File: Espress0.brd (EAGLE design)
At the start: 36.8 x 39.4 mm, 41 parts, among them CN1 4U#20329, Q2 reset, U1 AP2112K-3.3, U2 2MB Flash, U3 MCP73831T-2ACI/OT

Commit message: Add files via upload
* Fix micro USB grounding plane
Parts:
- moved CN1 0.38 mm to (18.4, 4.70)
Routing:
- net GND: track 8.82 -> 11.7 mm
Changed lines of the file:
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@@
 <attribute name="VALUE" x="19.177" y="12.319" size="0.4064" layer="121" ratio="10" rot="R90"/>
 </element>
-<element name="CN1" library="microbuilder" package="4UCONN_20329_V2" value="4U#20329" x="18.415" y="4.318"/>
+<element name="CN1" library="microbuilder" package="4UCONN_20329_V2" value="4U#20329" x="18.415" y="4.699"/>
 <element name="D2" library="adafruit" package="SOD-123FL" value="SCHOTTKY" x="23.622" y="10.668" smashed="yes" rot="R180">
 <attribute name="NAME" x="22.268" y="9.128" size="0.4064" layer="121"/>
@@
 </element>
 <element name="R1" library="microbuilder" package="0603-NO" value="1.5K" x="8.598803125" y="3.720196875" smashed="yes" rot="R269.6">
-<attribute name="NAME" x="9.9633375" y="5.520884375" size="0.6096" layer="25" font="vector" ratio="18" rot="R89.6"/>
-<attribute name="VALUE" x="8.08241875" y="5.51100625" size="0.4064" layer="121" font="vector" ratio="10" rot="R359.6"/>
+<attribute name="NAME" x="7.560115625" y="4.3753375" size="0.6096" layer="25" font="vector" ratio="18" rot="R179.6"/>
+<attribute name="VALUE" x="6.43141875" y="4.74900625" size="0.4064" layer="121" font="vector" ratio="10" rot="R359.6"/>
 </element>
 <element name="R4" library="microbuilder" package="0603-NO" value="10K" x="23.368" y="20.955" smashed="yes" rot="R180">
@@
 </element>
 <element name="R5" library="microbuilder" package="0603-NO" value="10K" x="7.239" y="7.747" smashed="yes" rot="R180">
-<attribute name="NAME" x="5.588" y="8.001" size="0.6096" layer="121" font="vector" ratio="18" rot="R180"/>
+<attribute name="NAME" x="5.715" y="9.017" size="0.6096" layer="121" font="vector" ratio="18" rot="R180"/>
 <attribute name="VALUE" x="7.62" y="6.985" size="0.4064" layer="121" font="vector" ratio="10" rot="R180"/>
 </element>
@@
 <element name="U2" library="microbuilder" package="SOIC8_208MIL" value="2MB Flash" x="9.652" y="11.684" smashed="yes" rot="R90">
 <attribute name="NAME" x="13.081" y="8.509" size="0.6096" layer="121" ratio="18" rot="R359.3"/>
-<attribute name="VALUE" x="7.239" y="15.113" size="0.4064" layer="121" ratio="10" rot="R180"/>
+<attribute name="VALUE" x="7.874" y="14.986" size="0.4064" layer="121" ratio="10" rot="R180"/>
 </element>
 <element name="PA22" library="testpad" package="B1,27" value="TPB1,27" x="13.716" y="7.62" smashed="yes">
-<attribute name="NAME" x="16.256" y="7.747" size="0.4064" layer="121" ratio="10" rot="R180"/>
+<attribute name="NAME" x="13.081" y="6.858" size="0.4064" layer="121" ratio="10" rot="R180"/>
 <attribute name="TP_SIGNAL_NAME" value="" x="13.081" y="5.715" size="1" layer="37"/>
 <attribute name="VALUE" x="13.081" y="6.858" size="0.0254" layer="27"/>
@@
 <via x="8.763" y="18.034" extent="1-16" drill="0.5"/>
 <via x="15.748" y="24.892" extent="1-16" drill="0.5"/>
-<wire x1="15.115" y1="5.218" x2="15.73768125" y2="5.103025" width="0.3048" layer="1"/>
 <wire x1="15.113" y1="25.908" x2="15.748" y2="24.892" width="0.508" layer="1"/>
 <via x="11.303" y="29.845" extent="1-16" drill="0.5"/>
-<wire x1="14.815" y1="2.418" x2="12.822" y2="2.418" width="0.508" layer="1"/>
-<wire x1="22.015" y1="2.418" x2="24.008" y2="2.418" width="0.508" layer="1"/>
-<wire x1="19.715" y1="5.093" x2="19.715" y2="4.094" width="0.4064" layer="1"/>
-<wire x1="19.165" y1="3.544" x2="19.165" y2="2.318" width="0.4064" layer="1"/>
+<wire x1="19.715" y1="5.474" x2="19.715" y2="4.094" width="0.4064" layer="1"/>
+<wire x1="19.165" y1="3.544" x2="19.165" y2="2.699" width="0.4064" layer="1"/>
 <wire x1="19.715" y1="4.094" x2="19.165" y2="3.544" width="0.4064" layer="1"/>
+<wire x1="19.265" y1="2.799" x2="19.165" y2="2.699" width="0.508" layer="1"/>
+<wire x1="14.815" y1="2.799" x2="14.815" y2="2.667" width="0.508" layer="1"/>
+<wire x1="22.015" y1="2.799" x2="14.815" y2="2.799" width="0.508" layer="1"/>
+<wire x1="19.715" y1="4.094" x2="22.015" y2="2.799" width="0" layer="19" extent="1-1"/>
 </signal>
 <signal name="D+">
 <contactref element="CN1" pad="D+"/>
 <contactref element="ATSAMD21E" pad="24"/>
-<wire x1="18.415" y1="13.716" x2="18.415" y2="5.093" width="0.3048" layer="1"/>
+<wire x1="18.415" y1="13.716" x2="18.415" y2="5.474" width="0.3048" layer="1"/>
 <wire x1="16.863" y1="23.408" x2="16.863" y2="15.268" width="0.3048" layer="1"/>
 <wire x1="16.863" y1="15.268" x2="18.415" y2="13.716" width="0.3048" layer="1"/>
@@
 <contactref element="ATSAMD21E" pad="23"/>
 <wire x1="16.363" y1="12.974" x2="17.8034" y2="11.5336" width="0.3556" layer="1"/>
-<wire x1="17.765" y1="5.093" x2="17.8034" y2="5.1314" width="0.3556" layer="1"/>
+<wire x1="17.765" y1="5.474" x2="17.8034" y2="5.1314" width="0.3556" layer="1"/>
 <wire x1="17.8034" y1="5.1314" x2="17.8034" y2="11.5336" width="0.3556" layer="1"/>
 <wire x1="16.363" y1="23.408" x2="16.363" y2="12.974" width="0.3048" layer="1"/>
@@
 <wire x1="30.099" y1="17.272" x2="27.559" y2="17.272" width="0.508" layer="16"/>
 <wire x1="17.115" y1="6.253" x2="16.51" y2="6.858" width="0.508" layer="1"/>
-<wire x1="17.115" y1="5.093" x2="17.115" y2="6.253" width="0.508" layer="1"/>
+<wire x1="17.115" y1="5.474" x2="17.115" y2="6.253" width="0.508" layer="1"/>
 <wire x1="27.559" y1="17.272" x2="20.955" y2="10.668" width="0.508" layer="16"/>
 <wire x1="20.955" y1="10.668" x2="19.939" y2="10.668" width="0.508" layer="16"/>
@@
 <wire x1="17.613" y1="24.658" x2="18.268" y2="24.658" width="0.3048" layer="1"/>
 <wire x1="18.268" y1="24.658" x2="18.669" y2="24.257" width="0.3048" layer="1"/>
-<wire x1="18.669" y1="24.257" x2="18.669" y2="20.193" width="0.3048" layer="1"/>
+<wire x1="18.669" y1="24.257" x2="18.669" y2="22.86" width="0.3048" layer="1"/>
+<wire x1="18.669" y1="22.86" x2="18.669" y2="20.193" width="0.3048" layer="1"/>
 <wire x1="18.669" y1="20.193" x2="24.003" y2="20.193" width="0.3048" layer="16"/>
 <wire x1="24.003" y1="20.193" x2="34.29" y2="30.48" width="0.3048" layer="16"/>
@@
 <contactref element="U2" pad="2"/>
 <contactref element="ATSAMD21E" pad="20"/>
-<wire x1="14.863" y1="23.408" x2="14.863" y2="11.43" width="0.3048" layer="1"/>
+<wire x1="14.863" y1="23.408" x2="14.863" y2="22.86" width="0.3048" layer="1"/>
+<wire x1="14.863" y1="22.86" x2="14.863" y2="11.43" width="0.3048" layer="1"/>
 <wire x1="13.843" y1="11.049" x2="12.967" y2="11.049" width="0.3556" layer="1"/>
 <wire x1="14.863" y1="11.43" x2="14.482" y2="11.049" width="0.3048" layer="1"/>
@@
 <wire x1="16.498" y1="11.188" x2="16.51" y2="10.922" width="0.3556" layer="16"/>
 <wire x1="16.51" y1="10.922" x2="16.51" y2="9.652" width="0.3556" layer="16"/>
-<wire x1="15.863" y1="23.408" x2="15.863" y2="11.823" width="0.254" layer="1"/>
+<wire x1="15.863" y1="23.408" x2="15.863" y2="22.86" width="0.254" layer="1"/>
+<wire x1="15.863" y1="22.86" x2="15.863" y2="11.823" width="0.254" layer="1"/>
 <wire x1="15.863" y1="11.823" x2="16.498" y2="11.188" width="0.254" layer="1"/>
 </signal>
@@
 <contactref element="PA22" pad="TP"/>
 <contactref element="ATSAMD21E" pad="21"/>
-<wire x1="15.363" y1="23.408" x2="15.363" y2="9.394" width="0.254" layer="1"/>
+<wire x1="15.363" y1="23.408" x2="15.363" y2="22.86" width="0.254" layer="1"/>
+<wire x1="15.363" y1="22.86" x2="15.363" y2="9.394" width="0.254" layer="1"/>
 <wire x1="15.363" y1="9.394" x2="13.716" y2="7.747" width="0.254" layer="1"/>
 <wire x1="13.716" y1="7.747" x2="13.716" y2="7.62" width="0.254" layer="1"/>
@@
 <via x="13.22" y="16.395" extent="1-16" drill="0.5"/>
 <wire x1="13.22" y1="16.395" x2="14.363" y2="17.538" width="0.254" layer="1"/>
-<wire x1="14.363" y1="17.538" x2="14.363" y2="23.408" width="0.254" layer="1"/>
+<wire x1="14.363" y1="17.538" x2="14.363" y2="22.86" width="0.254" layer="1"/>
+<wire x1="14.363" y1="22.86" x2="14.363" y2="23.408" width="0.254" layer="1"/>
 <wire x1="13.22" y1="16.395" x2="14.605" y2="15.01" width="0.3556" layer="16"/>
 <wire x1="14.605" y1="15.01" x2="14.605" y2="14.859" width="0.3556" layer="16"/>
@@
 <wire x1="19.558" y1="30.861" x2="28.956" y2="30.861" width="0.3556" layer="1"/>
 </signal>
+<signal name="N$3">
+<via x="19.685" y="8.255" extent="1-16" drill="0.35"/>
+</signal>
 </signals>

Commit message: Add files via upload
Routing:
- net GND: track 11.7 -> 10.4 mm
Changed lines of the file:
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@@
 <wire x1="19.265" y1="2.799" x2="19.165" y2="2.699" width="0.508" layer="1"/>
 <wire x1="14.815" y1="2.799" x2="14.815" y2="2.667" width="0.508" layer="1"/>
-<wire x1="22.015" y1="2.799" x2="14.815" y2="2.799" width="0.508" layer="1"/>
-<wire x1="19.715" y1="4.094" x2="22.015" y2="2.799" width="0" layer="19" extent="1-1"/>
+<wire x1="22.015" y1="2.799" x2="22.015" y2="2.699" width="0.508" layer="1"/>
+<wire x1="22.015" y1="2.699" x2="19.165" y2="2.699" width="0.508" layer="1"/>
+<wire x1="14.815" y1="2.799" x2="14.815" y2="2.699" width="0.508" layer="1"/>
+<wire x1="14.815" y1="2.699" x2="17.665" y2="2.699" width="0.508" layer="1"/>
 </signal>
 <signal name="D+">

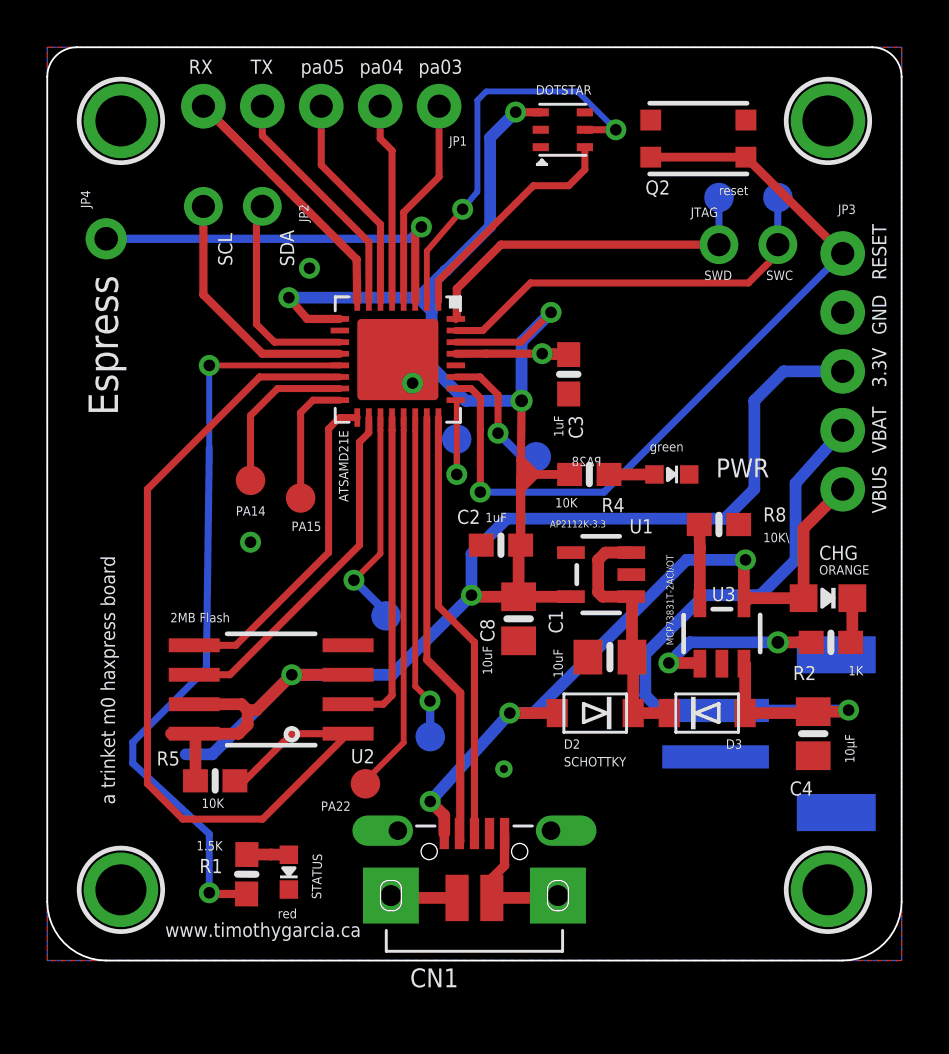
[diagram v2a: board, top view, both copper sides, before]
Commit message: Add files via upload
* SPI flash trace updates
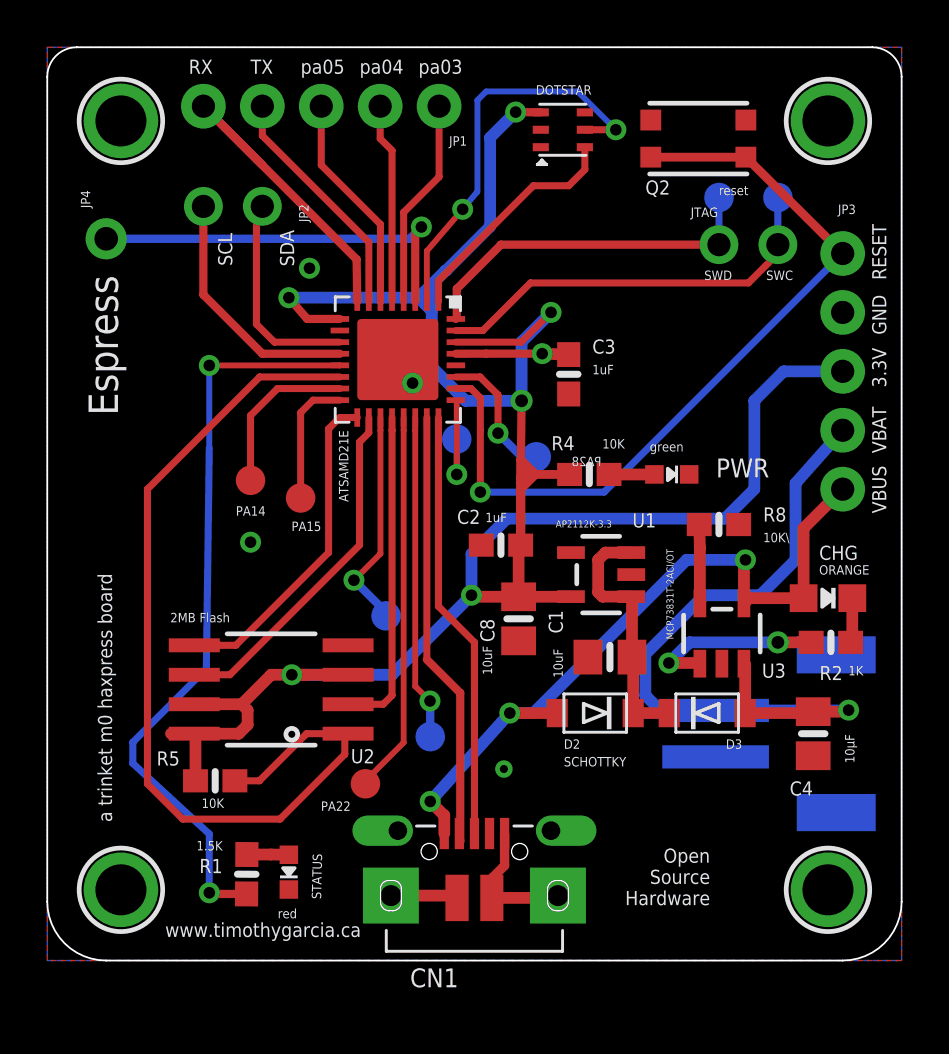
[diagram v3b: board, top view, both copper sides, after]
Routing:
- net 3.3V: track 107.2 -> 101.4 mm
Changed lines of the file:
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@@
 <text x="7.366" y="31.369" size="0.6096" layer="121" font="vector" rot="R270">SCL</text>
 <text x="3.048" y="23.495" size="1.27" layer="121" font="fixed" rot="R90">Espress</text>
-<text x="2.54" y="29.21" size="0.6096" layer="122" rot="MR270">Based on Trinket m0 by Adafruit Industries.</text>
+<text x="30.861" y="36.195" size="0.6096" layer="122" font="fixed" rot="MR0">Based on Trinket m0
+by Adafruit Industries.</text>
 <text x="31.496" y="1.143" size="0.6096" layer="122" rot="MR0">04/2018 - v0.3</text>
 <text x="5.08" y="1.016" size="0.6096" layer="121">www.timothygarcia.ca</text>
@@
 <text x="35.56" y="31.75" size="0.6096" layer="121" font="fixed" rot="R270">RESET</text>
 <text x="35.56" y="28.702" size="0.6096" layer="121" font="vector" rot="R270">GND</text>
-<text x="2.921" y="6.731" size="0.6096" layer="121" rot="R90">a trinket m0 haxpress board</text>
-<text x="3.81" y="29.21" size="0.6096" layer="122" rot="MR270.6">Designed for CircuitPython, but works with Arduino too!</text>
-<text x="30.861" y="37.338" size="0.6096" layer="122" rot="MR0">Open Source Hardware</text>
+<text x="2.794" y="5.969" size="0.6096" layer="121" rot="R90">a trinket m0 haxpress board</text>
+<text x="2.794" y="29.21" size="0.6096" layer="122" rot="MR270.6">Designed for CircuitPython, but works with Arduino too!</text>
+<text x="28.575" y="4.826" size="0.6096" layer="121" rot="R180">Open
+Source
+Hardware</text>
 <text x="35.56" y="21.336" size="0.6096" layer="121" font="fixed" rot="R270">VBUS</text>
 <wire x1="0" y1="2.54" x2="2.54" y2="0" width="0.0762" layer="20" curve="90"/>
@@
 </element>
 <element name="C3" library="microbuilder" package="0603-NO" value="1uF" x="22.479" y="25.273" smashed="yes" rot="R270">
-<attribute name="NAME" x="22.478996875" y="23.494996875" size="0.6096" layer="121" font="vector" ratio="18" rot="R270"/>
-<attribute name="VALUE" x="21.843996875" y="23.494996875" size="0.4064" layer="121" font="vector" ratio="10" rot="R270"/>
+<attribute name="NAME" x="23.495003125" y="26.161996875" size="0.6096" layer="121" font="vector" ratio="18"/>
+<attribute name="VALUE" x="23.495003125" y="25.272996875" size="0.4064" layer="121" font="vector" ratio="10"/>
 </element>
 <element name="C8" library="microbuilder" package="0805-NO" value="10uF" x="20.32" y="14.732" smashed="yes" rot="R270">
@@
 </element>
 <element name="R4" library="microbuilder" package="0603-NO" value="10K" x="23.368" y="20.955" smashed="yes" rot="R180">
-<attribute name="NAME" x="24.892" y="19.939" size="0.6096" layer="121" font="vector" ratio="18" rot="R180"/>
-<attribute name="VALUE" x="22.86" y="19.939" size="0.4064" layer="121" font="vector" ratio="10" rot="R180"/>
+<attribute name="NAME" x="22.733" y="22.606" size="0.6096" layer="121" font="vector" ratio="18" rot="R180"/>
+<attribute name="VALUE" x="24.892" y="22.479" size="0.4064" layer="121" font="vector" ratio="10" rot="R180"/>
 </element>
 <element name="R5" library="microbuilder" package="0603-NO" value="10K" x="7.239" y="7.747" smashed="yes" rot="R180">
@@
 </element>
 <element name="U1" library="microbuilder" package="SOT23-5" value="AP2112K-3.3" x="23.876" y="16.637" smashed="yes" rot="R90">
-<attribute name="NAME" x="25.092" y="18.415" size="0.6096" layer="25" ratio="18"/>
-<attribute name="VALUE" x="21.663" y="18.669" size="0.3048" layer="121" ratio="10"/>
+<attribute name="NAME" x="25.219" y="18.669" size="0.6096" layer="25" ratio="18"/>
+<attribute name="VALUE" x="21.917" y="18.669" size="0.3048" layer="121" ratio="10"/>
 </element>
 <element name="U2" library="microbuilder" package="SOIC8_208MIL" value="2MB Flash" x="9.652" y="11.684" smashed="yes" rot="R90">
@@
 </element>
 <element name="U3" library="microbuilder" package="SOT23-5" value="MCP73831T-2ACI/OT" x="29.083" y="14.097" smashed="yes">
-<attribute name="NAME" x="28.648" y="15.494" size="0.6096" layer="121" ratio="18"/>
-<attribute name="VALUE" x="26.997" y="13.589" size="0.3048" layer="121" ratio="10" rot="R90"/>
+<attribute name="NAME" x="30.807" y="12.192" size="0.6096" layer="121" ratio="18"/>
+<attribute name="VALUE" x="26.997" y="13.843" size="0.3048" layer="121" ratio="10" rot="R90"/>
 </element>
 <element name="CHG" library="microbuilder" package="CHIPLED_0805_NOOUTLINE" value="ORANGE" x="33.655" y="15.621" smashed="yes" rot="R270">
@@
 </element>
 <element name="R2" library="microbuilder" package="0603-NO" value="1K" x="33.782" y="13.716" smashed="yes" rot="R180">
-<attribute name="NAME" x="33.147" y="12.7" size="0.6096" layer="121" font="vector" ratio="18" rot="R180"/>
+<attribute name="NAME" x="34.29" y="12.7" size="0.6096" layer="121" font="vector" ratio="18" rot="R180"/>
 <attribute name="VALUE" x="35.179" y="12.7" size="0.4064" layer="121" font="vector" ratio="10" rot="R180"/>
 </element>
@@
 <wire x1="19.715" y1="4.094" x2="19.165" y2="3.544" width="0.4064" layer="1"/>
 <wire x1="19.265" y1="2.799" x2="19.165" y2="2.699" width="0.508" layer="1"/>
-<wire x1="14.815" y1="2.799" x2="14.815" y2="2.667" width="0.508" layer="1"/>
 <wire x1="22.015" y1="2.799" x2="22.015" y2="2.699" width="0.508" layer="1"/>
 <wire x1="22.015" y1="2.699" x2="19.165" y2="2.699" width="0.508" layer="1"/>
-<wire x1="14.815" y1="2.799" x2="14.815" y2="2.699" width="0.508" layer="1"/>
-<wire x1="14.815" y1="2.699" x2="17.665" y2="2.699" width="0.508" layer="1"/>
+<wire x1="14.815" y1="2.799" x2="17.665" y2="2.799" width="0.508" layer="1"/>
+<wire x1="17.665" y1="2.799" x2="17.665" y2="2.699" width="0.508" layer="1"/>
 </signal>
 <signal name="D+">
@@
 <via x="20.447" y="24.13" extent="1-16" drill="0.55"/>
 <contactref element="JP3" pad="3"/>
-<wire x1="10.541" y1="12.319" x2="7.112" y2="8.89" width="0.508" layer="16"/>
-<wire x1="7.112" y1="8.89" x2="5.969" y2="8.89" width="0.508" layer="16"/>
 <via x="20.193" y="36.576" extent="1-16" drill="0.5"/>
 <wire x1="21.275" y1="36.564" x2="20.193" y2="36.576" width="0.3556" layer="1"/>
@@
 <wire x1="8.636" y1="10.16" x2="8.255" y2="9.779" width="0.508" layer="1"/>
 <wire x1="8.255" y1="9.779" x2="6.337" y2="9.779" width="0.508" layer="1"/>
-<wire x1="10.541" y1="12.319" x2="9.017" y2="10.795" width="0.508" layer="1"/>
-<wire x1="9.017" y1="10.795" x2="8.636" y2="10.795" width="0.508" layer="1"/>
 <wire x1="16.5735" y1="28.0035" x2="16.5735" y2="25.5905" width="0.508" layer="16"/>
 <wire x1="16.5735" y1="25.5905" x2="18.034" y2="24.13" width="0.508" layer="16"/>
 <wire x1="18.034" y1="24.13" x2="20.447" y2="24.13" width="0.508" layer="16"/>
+<wire x1="8.382" y1="11.049" x2="9.652" y2="12.319" width="0.508" layer="1"/>
+<wire x1="9.652" y1="12.319" x2="10.541" y2="12.319" width="0.508" layer="1"/>
 </signal>
 <signal name="D1_A0_PA02">
@@
 <contactref element="R5" pad="1"/>
 <contactref element="ATSAMD21E" pad="14"/>
-<wire x1="8.509" y1="7.747" x2="8.089" y2="7.747" width="0.3048" layer="1"/>
 <wire x1="12.613" y1="25.158" x2="9.156" y2="25.158" width="0.3048" layer="1"/>
-<wire x1="12.967" y1="9.779" x2="10.541" y2="9.779" width="0.3048" layer="1"/>
-<wire x1="10.541" y1="9.779" x2="8.509" y2="7.747" width="0.3048" layer="1"/>
 <wire x1="9.156" y1="25.158" x2="4.318" y2="20.32" width="0.3048" layer="1"/>
-<wire x1="6.35" y1="6.096" x2="9.284" y2="6.096" width="0.3048" layer="1"/>
-<wire x1="9.284" y1="6.096" x2="12.967" y2="9.779" width="0.3048" layer="1"/>
 <wire x1="4.318" y1="20.32" x2="4.318" y2="7.62" width="0.3048" layer="1"/>
-<wire x1="4.318" y1="7.62" x2="5.842" y2="6.096" width="0.3048" layer="1"/>
-<wire x1="5.842" y1="6.096" x2="6.35" y2="6.096" width="0.3048" layer="1"/>
+<wire x1="5.842" y1="6.096" x2="4.318" y2="7.62" width="0.3048" layer="1"/>
+<wire x1="8.089" y1="7.747" x2="9.144" y2="7.747" width="0.3048" layer="1"/>
+<wire x1="9.144" y1="7.747" x2="11.176" y2="9.779" width="0.3048" layer="1"/>
+<wire x1="11.176" y1="9.779" x2="12.967" y2="9.779" width="0.3048" layer="1"/>
+<wire x1="12.967" y1="9.779" x2="12.827" y2="9.639" width="0.3048" layer="1"/>
+<wire x1="12.827" y1="9.639" x2="12.827" y2="8.89" width="0.3048" layer="1"/>
+<wire x1="12.827" y1="8.89" x2="10.033" y2="6.096" width="0.3048" layer="1"/>
+<wire x1="10.033" y1="6.096" x2="5.842" y2="6.096" width="0.3048" layer="1"/>
 </signal>
 <signal name="PA19D_FLASHMISO">
@@
 </drawing>
 <compatibility>
+<note version="6.3" minversion="6.2.2" severity="warning">
+Since Version 6.2.2 text objects can contain more than one line,
+which will not be processed correctly with this version.
+</note>
 <note version="8.2" severity="warning">
 Since Version 8.2, EAGLE supports online libraries. The ids

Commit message: Add files via upload
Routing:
- net 3.3V: track 101.4 -> 101.9 mm
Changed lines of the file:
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@@
 <wire x1="19.0897875" y1="35.4727875" x2="19.0897875" y2="31.6399" width="0.508" layer="16"/>
 <wire x1="6.337" y1="11.049" x2="8.382" y2="11.049" width="0.508" layer="1"/>
-<wire x1="8.382" y1="11.049" x2="8.636" y2="10.795" width="0.508" layer="1"/>
+<wire x1="8.636" y1="10.795" x2="8.382" y2="11.049" width="0.508" layer="1"/>
 <wire x1="8.636" y1="10.795" x2="8.636" y2="10.16" width="0.508" layer="1"/>
 <wire x1="8.636" y1="10.16" x2="8.255" y2="9.779" width="0.508" layer="1"/>
@@
 <wire x1="16.5735" y1="25.5905" x2="18.034" y2="24.13" width="0.508" layer="16"/>
 <wire x1="18.034" y1="24.13" x2="20.447" y2="24.13" width="0.508" layer="16"/>
-<wire x1="8.382" y1="11.049" x2="9.652" y2="12.319" width="0.508" layer="1"/>
+<wire x1="8.382" y1="11.049" x2="8.636" y2="11.303" width="0.508" layer="1"/>
+<wire x1="8.636" y1="11.303" x2="8.8265" y2="11.4935" width="0.508" layer="1"/>
+<wire x1="8.8265" y1="11.4935" x2="9.652" y2="12.319" width="0.508" layer="1"/>
 <wire x1="9.652" y1="12.319" x2="10.541" y2="12.319" width="0.508" layer="1"/>
+<wire x1="8.636" y1="10.795" x2="8.636" y2="11.303" width="0.508" layer="1"/>
 </signal>
 <signal name="D1_A0_PA02">
